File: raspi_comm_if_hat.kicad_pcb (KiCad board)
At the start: 2 copper layers, 65 x 56 mm, 18 parts, among them J1 Conn_01x04, J2 Conn_01x04, J3 Conn_01x04, J4 Conn_02x20_Odd_Even, Q1 Q_PMOS_GSD, Q2 Q_PMOS_GSD, U1 MCP25625-x-SS, Y1 Resonator_Small

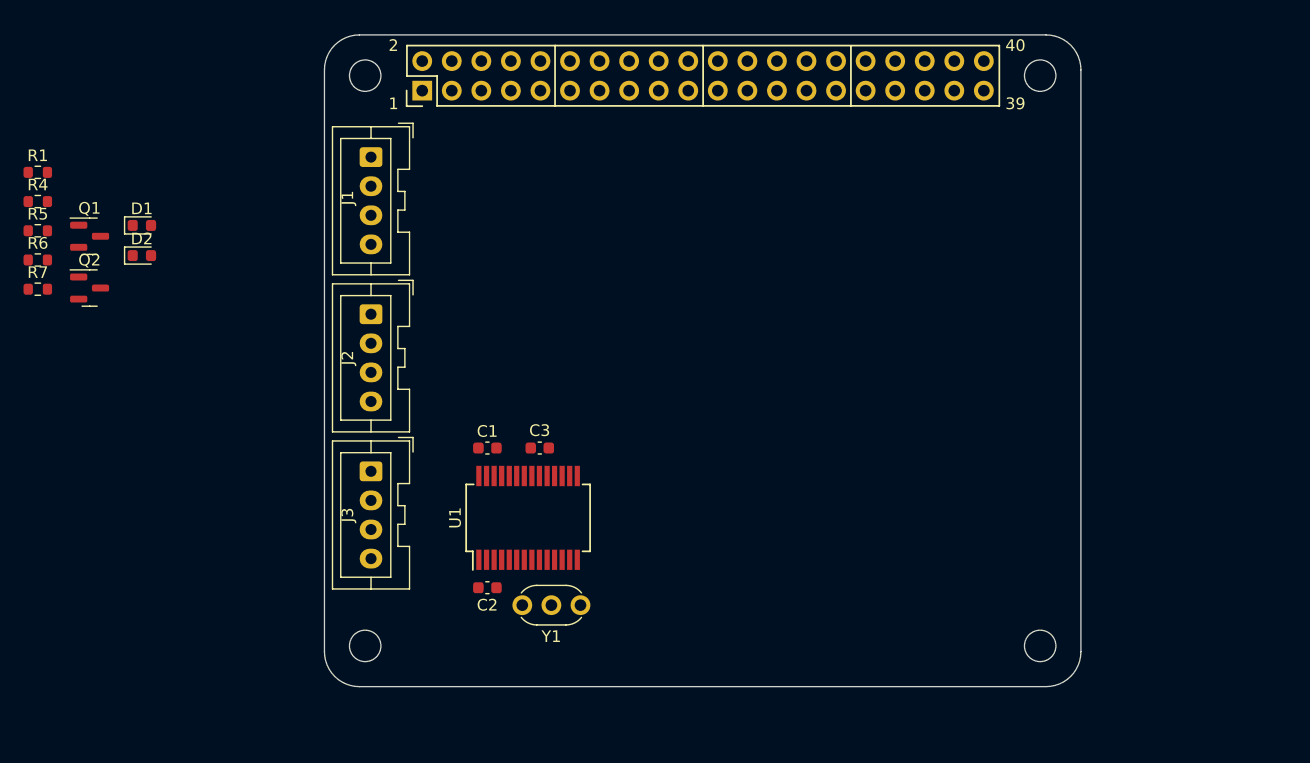
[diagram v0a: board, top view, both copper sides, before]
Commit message: draw schemtic & PCB
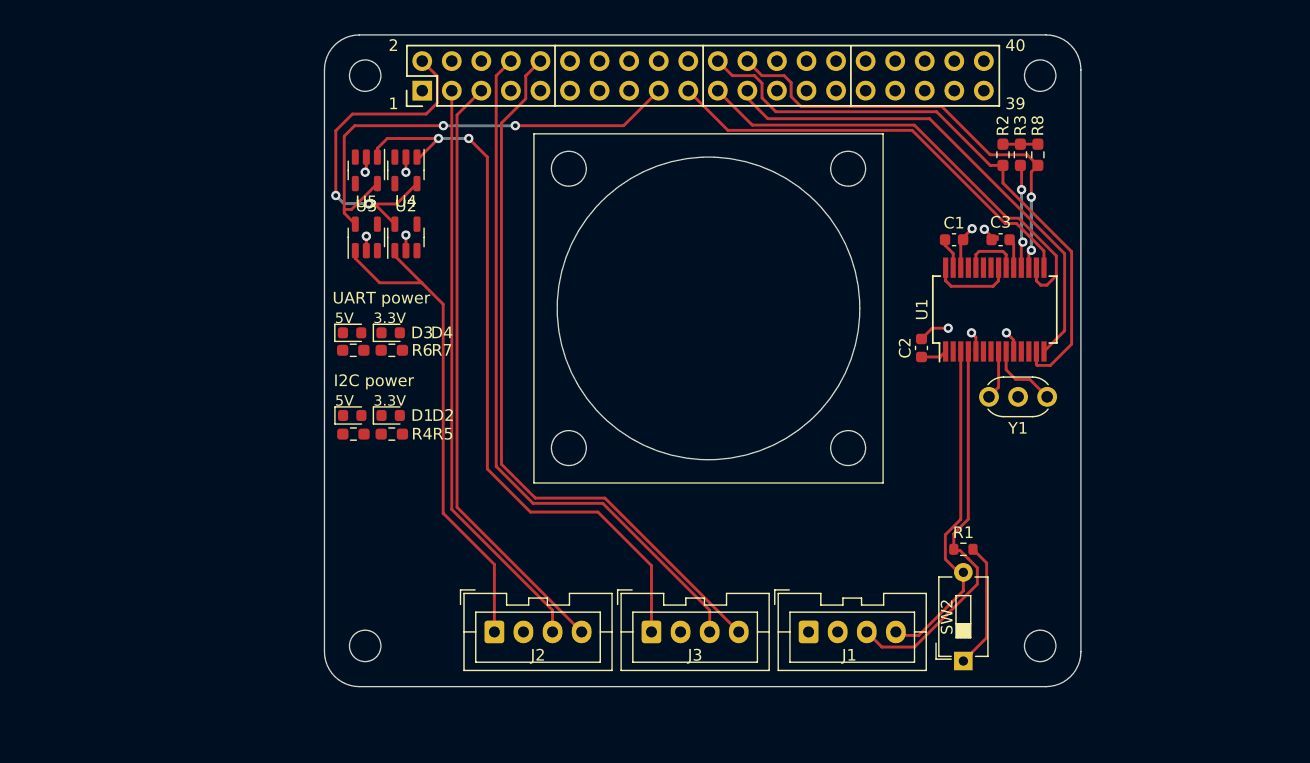
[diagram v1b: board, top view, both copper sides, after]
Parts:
- removed Q1, Q2: Q_PMOS_GSD, Package_TO_SOT_SMD:SOT-23
- added D3: LED, LED_SMD:LED_0603_1608Metric, F.Cu at (102.4, 76.6)
- added D4: LED, LED_SMD:LED_0603_1608Metric, F.Cu at (105.7, 76.6)
- added R2: 10k, Resistor_SMD:R_0603_1608Metric_Pad0.98x0.95mm_HandSolder, F.Cu at (158.3, 61.3)
- added R3: 10k, Resistor_SMD:R_0603_1608Metric_Pad0.98x0.95mm_HandSolder, F.Cu at (159.8, 61.3)
- added R8: 10k, Resistor_SMD:R_0603_1608Metric_Pad0.98x0.95mm_HandSolder, F.Cu at (161.3, 61.3)
- added SW2: SW_DIP_x01, Button_Switch_THT:SW_DIP_SPSTx01_Slide_6.7x4.1mm_W7.62mm_P2.54mm_LowProfile, F.Cu at (154.9, 104.8)
- added U2: TCK107AF, Package_TO_SOT_SMD:SOT-23-5, F.Cu at (107.0, 68.4)
- added U3: TCK107AF, Package_TO_SOT_SMD:SOT-23-5, F.Cu at (103.6, 68.4)
- added U4: TCK107AF, Package_TO_SOT_SMD:SOT-23-5, F.Cu at (107.0, 62.6)
- added U5: TCK107AF, Package_TO_SOT_SMD:SOT-23-5, F.Cu at (103.6, 62.6)
- J1, J2, J3: value Conn_01x04 -> B04B-XA
- R4, R5, R6, R7: value 4.7k -> 1k; footprint Resistor_SMD:R_0603_1608Metric -> Resistor_SMD:R_0603_1608Metric_Pad0.98x0.95mm_HandSolder
- Y1: value Resonator_Small -> 20MHz
- moved R1 85.9 mm to (154.9, 95.2)
- moved J1 55.5 mm to (141.6, 102.3), turned to 0 degrees
- moved C1 43.9 mm to (154.1, 68.6)
- moved U1 43.9 mm to (157.6, 74.6)
- moved Y1 43.9 mm to (162.1, 82.1)
- moved C3 43.5 mm to (158.1, 68.6)
- moved C2 42.6 mm to (151.3, 77.9), turned to 90 degrees
- moved R5 35.1 mm to (105.8, 85.3)
- moved R4 33.7 mm to (102.5, 85.3)
- moved R7 30.9 mm to (105.8, 78.1)
- moved J2 29.3 mm to (114.6, 102.3), turned to 0 degrees
- moved R6 28.2 mm to (102.5, 78.1)
- moved J3 27.8 mm to (128.1, 102.3), turned to 0 degrees
- moved D2 25.4 mm to (105.7, 83.7)
- moved D1 24.4 mm to (102.4, 83.7)
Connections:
- C2 pad 1: +3V3 -> +3.3V
- C3 pad 1: +3V3 -> +3.3V
- D1 pad 1: unconnected-(D1-K-Pad1) -> Net-(D1-K)
- D2 pad 1: unconnected-(D2-K-Pad1) -> Net-(D2-K)
- J1 pad 1: unconnected-(J1-Pin_1-Pad1) -> GND
- J1 pad 2: GND -> +12V
- J2 pad 1: unconnected-(J2-Pin_1-Pad1) -> I2C_PWR
- J2 pad 2: unconnected-(J2-Pin_2-Pad2) -> GND
- J2 pad 3: unconnected-(J2-Pin_3-Pad3) -> SDA
- J2 pad 4: unconnected-(J2-Pin_4-Pad4) -> SDL
- J3 pad 1: unconnected-(J3-Pin_1-Pad1) -> UART_PWR
- J3 pad 2: unconnected-(J3-Pin_2-Pad2) -> GND
- J3 pad 3: unconnected-(J3-Pin_3-Pad3) -> TX
- J3 pad 4: unconnected-(J3-Pin_4-Pad4) -> RX
- J4 pad 10: unconnected-(J4-Pin_10-Pad10) -> RX
- J4 pad 14: unconnected-(J4-Pin_14-Pad14) -> GND
- J4 pad 17: unconnected-(J4-Pin_17-Pad17) -> +3.3V
- J4 pad 19: unconnected-(J4-Pin_19-Pad19) -> MOSI
- J4 pad 2: unconnected-(J4-Pin_2-Pad2) -> +5V
- J4 pad 21: unconnected-(J4-Pin_21-Pad21) -> MISO
- J4 pad 22: unconnected-(J4-Pin_22-Pad22) -> CAN_INT
- J4 pad 23: unconnected-(J4-Pin_23-Pad23) -> CLK
- J4 pad 24: unconnected-(J4-Pin_24-Pad24) -> CS
- J4 pad 3: unconnected-(J4-Pin_3-Pad3) -> SDA
- J4 pad 34: unconnected-(J4-Pin_34-Pad34) -> GND
- J4 pad 5: unconnected-(J4-Pin_5-Pad5) -> SDL
- J4 pad 6: unconnected-(J4-Pin_6-Pad6) -> GND
- J4 pad 8: unconnected-(J4-Pin_8-Pad8) -> TX
- R4 pad 1: +5V -> Net-(D1-K)
- R4 pad 2: Net-(Q1-G) -> GND
- R5 pad 1: Net-(Q1-G) -> Net-(D2-K)
- R5 pad 2: Net-(SW1-A) -> GND
- R6 pad 1: +3V3 -> Net-(D3-K)
- R6 pad 2: Net-(Q2-G) -> GND
- R7 pad 1: Net-(Q2-G) -> Net-(D4-K)
- R7 pad 2: Net-(SW1-C) -> GND
- U1 pad 1: +3V3 -> +3.3V
- U1 pad 13: unconnected-(U1-~{INT}-Pad13) -> CAN_INT
- U1 pad 14: unconnected-(U1-SCK-Pad14) -> CLK
- U1 pad 15: unconnected-(U1-SI-Pad15) -> MOSI
- U1 pad 16: unconnected-(U1-SO-Pad16) -> MISO
- U1 pad 17: unconnected-(U1-~{CS}-Pad17) -> CS
- U1 pad 18: unconnected-(U1-~{RESET}-Pad18) -> Net-(U1-~{RESET})
- U1 pad 19: +3V3 -> +3.3V
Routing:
- net UART_PWR: track 0.00 -> 63.8 mm, vias 0 -> 2
- net RX: track 0.00 -> 62.4 mm
- net TX: track 0.00 -> 60.7 mm
- net SDL: track 0.00 -> 51.8 mm
- net CAN_INT: track 0.00 -> 51.7 mm
- net SDA: track 0.00 -> 50.1 mm
- net +3.3V: track 0.00 -> 48.2 mm, vias 0 -> 2
- net I2C_PWR: track 0.00 -> 43.5 mm
- net CLK: track 0.00 -> 42.6 mm
- net MISO: track 0.00 -> 40.0 mm
- net CS: track 0.00 -> 38.5 mm, vias 0 -> 2
- net MOSI: track 0.00 -> 37.7 mm
- net Net-(J1-Pin_3): track 0.00 -> 33.9 mm
- net +5V: track 0.00 -> 33.1 mm, vias 0 -> 2
- net Net-(J1-Pin_4): track 0.00 -> 29.5 mm
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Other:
- outline, holes or cut-outs redrawn
- board text added: "3.3V"
- board text added: "5V"
- board text added: "I2C power"
- board text added: "UART power"

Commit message: update pcb
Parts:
- added H1: MountingHole, MountingHole:MountingHole_2.7mm_M2.5, F.Cu at (103.5, 54.5)
- added H2: MountingHole, MountingHole:MountingHole_2.7mm_M2.5, F.Cu at (161.5, 54.5)
- added H3: MountingHole, MountingHole:MountingHole_2.7mm_M2.5, F.Cu at (103.5, 103.5)
- added H4: MountingHole, MountingHole:MountingHole_2.7mm_M2.5, F.Cu at (161.5, 103.5)
- added SW1: SW_SPDT, Button_Switch_THT:SW_CuK_OS102011MA1QN1_SPDT_Angled, F.Cu at (103.5, 90.3)
- added SW3: SW_SPDT, Button_Switch_THT:SW_CuK_OS102011MA1QN1_SPDT_Angled, F.Cu at (103.5, 76.7)
- U2, U3, U4, U5: value TCK107AF -> TCK106AF
- moved D2 10.5 mm to (108.7, 93.8), turned to -90 degrees
- moved D1 9.28 mm to (108.7, 90.5), turned to -90 degrees
- moved R5 8.70 mm to (107.1, 93.9), turned to -90 degrees
- moved R4 7.03 mm to (107.1, 90.6), turned to -90 degrees
- moved D3 6.25 mm to (108.6, 77.1), turned to -90 degrees
- moved D4 4.80 mm to (108.6, 80.4), turned to -90 degrees
- moved R6 4.71 mm to (107.1, 77.2), turned to -90 degrees
- moved R7 2.75 mm to (107.1, 80.5), turned to -90 degrees
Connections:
- J4 pad 1: unconnected-(J4-Pin_1-Pad1) -> +3.3V
- J4 pad 25: unconnected-(J4-Pin_25-Pad25) -> GND
- J4 pad 30: unconnected-(J4-Pin_30-Pad30) -> GND
- J4 pad 39: unconnected-(J4-Pin_39-Pad39) -> GND
- J4 pad 9: unconnected-(J4-Pin_9-Pad9) -> GND
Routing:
- net +5V: track 33.1 -> 153.5 mm, vias 2 -> 7
- net +3.3V: track 48.2 -> 89.3 mm, vias 2 -> 3
- net Net-(D1-A): track 0.00 -> 35.7 mm, vias 0 -> 2
- net Net-(D4-A): track 0.00 -> 32.9 mm, vias 0 -> 4
- net Net-(D2-A): track 0.00 -> 32.0 mm, vias 0 -> 2
- net Net-(D3-A): track 0.00 -> 24.8 mm, vias 0 -> 4
- net GND: track 16.4 -> 20.6 mm, vias 9 -> 13
- net Net-(D2-K): track 0.00 -> 1.61 mm
- net Net-(D1-K): track 0.00 -> 1.61 mm
- net Net-(D4-K): track 0.00 -> 1.51 mm
- net Net-(D3-K): track 0.00 -> 1.51 mm
- net UART_PWR: track 63.8 -> 64.5 mm
- added copper zone on B.Cu, net GND
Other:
- outline, holes or cut-outs redrawn

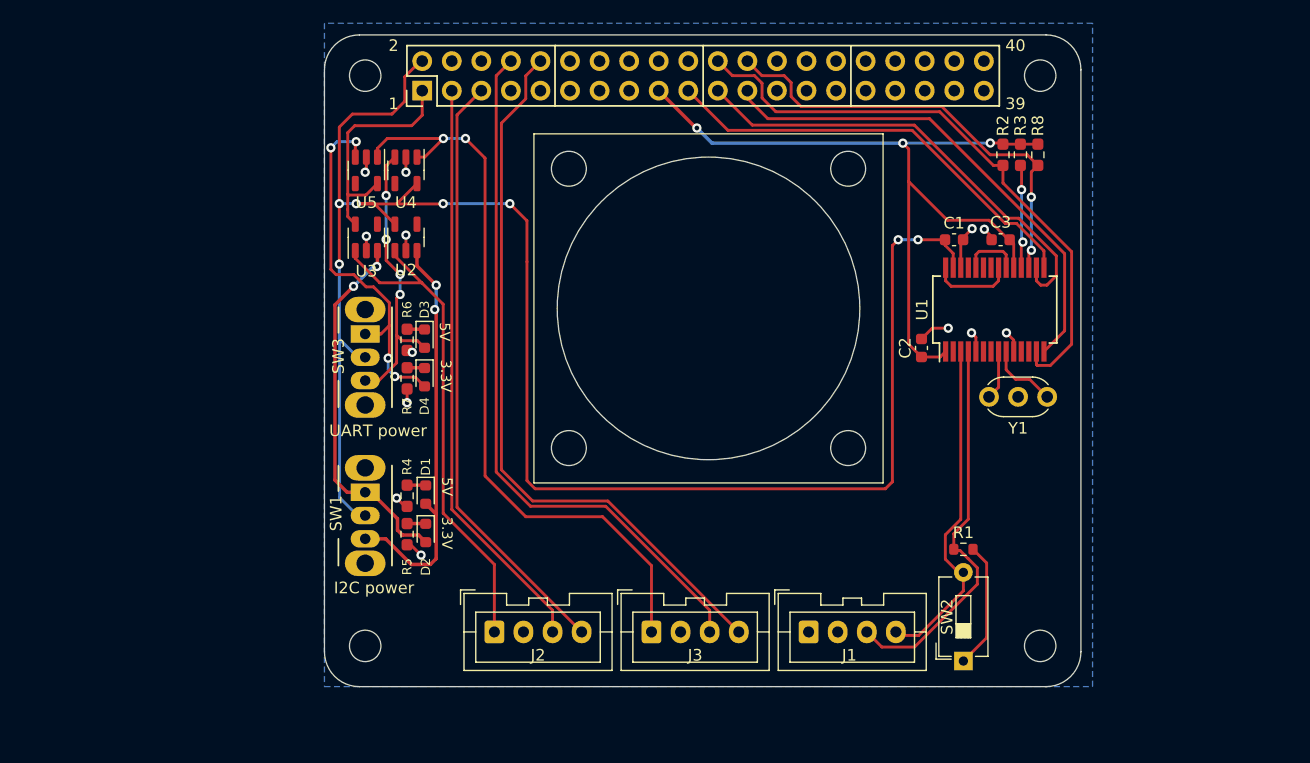
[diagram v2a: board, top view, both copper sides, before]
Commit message: add fan connector
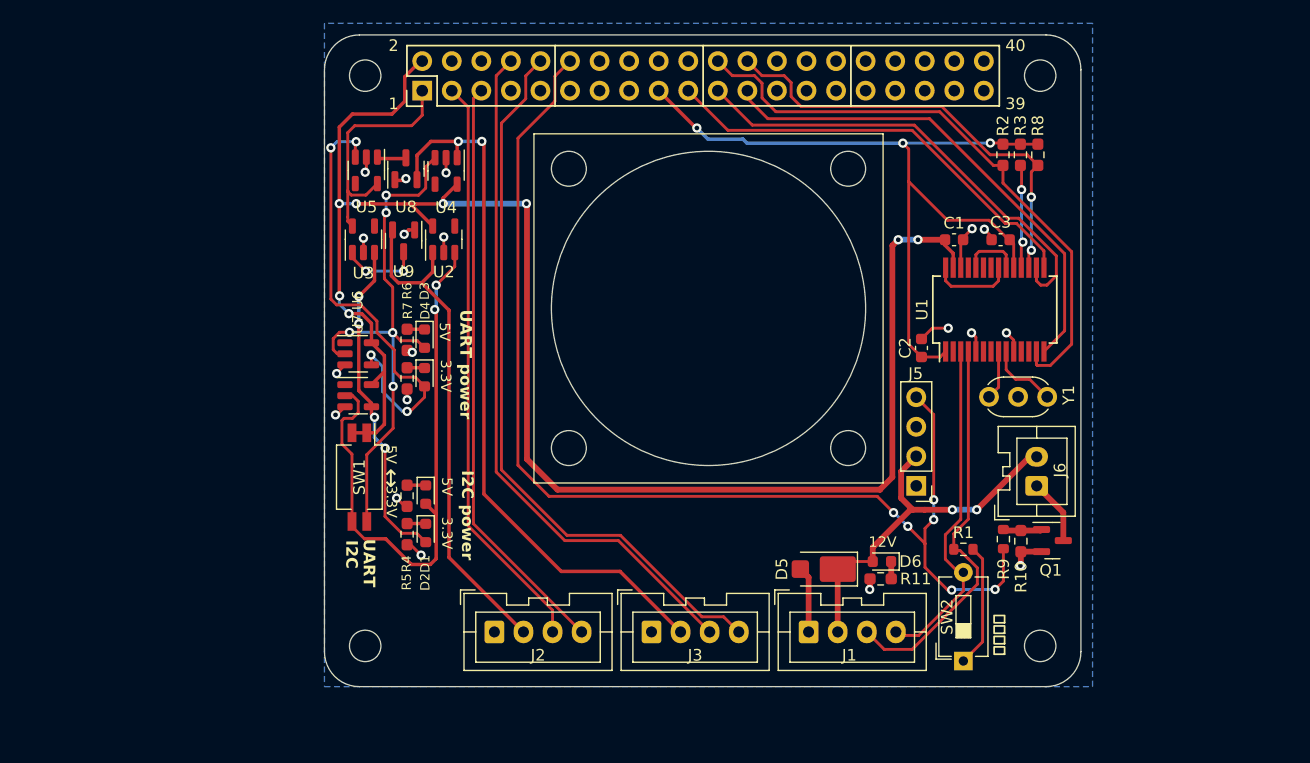
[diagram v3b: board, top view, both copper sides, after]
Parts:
- removed SW3: SW_SPDT, Button_Switch_THT:SW_CuK_OS102011MA1QN1_SPDT_Angled
- added D5: D_Schottky, Diode_SMD:Vishay_SMPA, F.Cu at (142.9, 96.9)
- added D6: LED, LED_SMD:LED_0603_1608Metric, F.Cu at (147.9, 96.2)
- added J5: Conn_01x04, Connector_PinHeader_2.54mm:PinHeader_1x04_P2.54mm_Vertical, F.Cu at (150.8, 89.8)
- added J6: Conn_01x02, Connector_JST:JST_XA_B02B-XASK-1_1x02_P2.50mm_Vertical, F.Cu at (161.2, 89.8)
- added Q1: Q_NMOS_GSD, Package_TO_SOT_SMD:SOT-23, F.Cu at (162.6, 94.5)
- added R10: 10k, Resistor_SMD:R_0603_1608Metric_Pad0.98x0.95mm_HandSolder, F.Cu at (159.8, 94.5)
- added R11: 10k, Resistor_SMD:R_0603_1608Metric_Pad0.98x0.95mm_HandSolder, F.Cu at (147.8, 97.7)
- added R9: 120, Resistor_SMD:R_0603_1608Metric, F.Cu at (158.3, 94.3)
- added U6: 74AHC1G04, Package_TO_SOT_SMD:SOT-23-5, F.Cu at (102.9, 78.4)
- added U7: 74AHC1G04, Package_TO_SOT_SMD:SOT-23-5, F.Cu at (102.9, 82.0)
- added U8: CH213K, Package_TO_SOT_SMD:SOT-23, F.Cu at (107.0, 62.5)
- added U9: CH213K, Package_TO_SOT_SMD:SOT-23, F.Cu at (106.8, 68.7)
- SW1: value SW_SPDT -> SW_DIP_x02; footprint Button_Switch_THT:SW_CuK_OS102011MA1QN1_SPDT_Angled -> Button_Switch_SMD:SW_DIP_SPSTx02_Slide_Copal_CHS-02B_W7.62mm_P1.27mm
- moved U4 3.45 mm to (110.5, 62.7)
- moved U2 3.25 mm to (110.2, 68.6)
- moved SW1 1.39 mm to (103.0, 89.0)
- moved U3 0.30 mm to (103.3, 68.6)
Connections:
- J2 pad 1: I2C_PWR -> GND
- J2 pad 2: GND -> I2C_PWR
- J3 pad 1: UART_PWR -> GND
- J3 pad 2: GND -> UART_PWR
- J4 pad 12: unconnected-(J4-Pin_12-Pad12) -> FAN_PWM
- SW1 pad 1: Net-(D2-A) -> +5V
- U3 pad 1: I2C_PWR -> Net-(U3-OUT)
- U5 pad 1: UART_PWR -> Net-(U5-OUT)
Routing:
- net FAN_PWM: track 0.00 -> 100.6 mm, vias 0 -> 6
- net +12V: track 0.00 -> 32.7 mm, vias 0 -> 2
- net Net-(D3-A): track 24.8 -> 46.9 mm, vias 4 -> 5
- net Net-(D1-A): track 35.7 -> 51.0 mm
- net GND: track 20.6 -> 34.2 mm, vias 13 -> 19
- net Net-(U3-OUT): track 0.00 -> 7.07 mm, vias 0 -> 2
- net Net-(D4-A): track 32.9 -> 39.8 mm
- net Net-(J6-Pin_1): track 0.00 -> 5.65 mm
- net +5V: track 153.5 -> 148.0 mm, vias 7 -> 8
- net Net-(D2-A): track 32.0 -> 28.6 mm, vias 2 -> 4
- net Net-(Q1-G): track 0.00 -> 3.35 mm
- net UART_PWR: track 64.5 -> 61.8 mm
- net Net-(U5-OUT): track 0.00 -> 2.50 mm
- net Net-(D6-K): track 0.00 -> 1.50 mm
- net SDL: track 51.8 -> 50.6 mm
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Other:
- outline, holes or cut-outs redrawn
- board text added: "12V"
- board text added: "I2C"
- board text added: "UART"
- board text added: "↔"
- board text added: "終端抵抗"

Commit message: v0.1.0
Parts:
- added C1: 10uF, Capacitor_SMD:C_0603_1608Metric, F.Cu at (104.0, 61.5)
- added C2: 10uF, Capacitor_SMD:C_0603_1608Metric, F.Cu at (108.9, 61.5)
- added C3: 0.1uF, Capacitor_SMD:C_0603_1608Metric, F.Cu at (114.4, 92.8)
- added C4: 100uF, Capacitor_Tantalum_SMD:CP_EIA-7343-15_Kemet-W, F.Cu at (141.5, 95.9)
- added C8: 0.1uF, Capacitor_SMD:C_0603_1608Metric, F.Cu at (110.8, 100.8)
- added C9: 0.1uF, Capacitor_SMD:C_0603_1608Metric, F.Cu at (124.5, 100.5)
- added Q2: Q_NMOS_GSD, Package_TO_SOT_SMD:SOT-23, F.Cu at (117.5, 99.8)
- added Q3: Q_NMOS_GSD, Package_TO_SOT_SMD:SOT-23, F.Cu at (117.5, 96.5)
- added Q4: Q_NMOS_GSD, Package_TO_SOT_SMD:SOT-23, F.Cu at (131.0, 99.9)
- added Q5: Q_NMOS_GSD, Package_TO_SOT_SMD:SOT-23, F.Cu at (131.0, 96.5)
- added R14: 10k, Resistor_SMD:R_0603_1608Metric_Pad0.98x0.95mm_HandSolder, F.Cu at (114.8, 96.5)
- added R15: 10k, Resistor_SMD:R_0603_1608Metric_Pad0.98x0.95mm_HandSolder, F.Cu at (114.8, 99.9)
- added R16: 10k, Resistor_SMD:R_0603_1608Metric_Pad0.98x0.95mm_HandSolder, F.Cu at (120.2, 99.9)
- added R17: 10k, Resistor_SMD:R_0603_1608Metric_Pad0.98x0.95mm_HandSolder, F.Cu at (120.2, 96.5)
- added R18: 10k, Resistor_SMD:R_0603_1608Metric_Pad0.98x0.95mm_HandSolder, F.Cu at (128.4, 96.5)
- added R19: 10k, Resistor_SMD:R_0603_1608Metric_Pad0.98x0.95mm_HandSolder, F.Cu at (128.4, 100.0)
- added R20: 10k, Resistor_SMD:R_0603_1608Metric_Pad0.98x0.95mm_HandSolder, F.Cu at (133.7, 100.0)
- added R21: 10k, Resistor_SMD:R_0603_1608Metric_Pad0.98x0.95mm_HandSolder, F.Cu at (133.7, 96.5)
- added R7: 10k, Resistor_SMD:R_0603_1608Metric_Pad0.98x0.95mm_HandSolder, F.Cu at (110.6, 99.2)
- added R8: 10k, Resistor_SMD:R_0603_1608Metric_Pad0.98x0.95mm_HandSolder, F.Cu at (124.3, 99.0)
- added REF**: KiCad-Logo2_5mm_SilkScreen, Symbol:KiCad-Logo2_5mm_SilkScreen, F.Cu at (156.7, 67.7)
- moved SW2 3.07 mm to (102.3, 92.0)
- moved C5 3.00 mm to (158.1, 71.6)
- moved C6 3.00 mm to (151.3, 80.9)
- moved C7 3.00 mm to (154.1, 71.6)
- moved D1 3.00 mm to (147.9, 99.2)
- moved D2 3.00 mm to (142.9, 99.9)
- moved D5 3.00 mm to (108.6, 80.1)
- moved D6 3.00 mm to (108.6, 83.4)
- moved H1 3.00 mm to (103.5, 57.5)
- moved H2 3.00 mm to (161.5, 57.5)
- moved H3 3.00 mm to (103.5, 106.5)
- moved H4 3.00 mm to (161.5, 106.5)
- moved J1 3.00 mm to (141.6, 105.3)
- moved J2 3.00 mm to (108.4, 58.8)
- moved J3 3.00 mm to (114.6, 105.3)
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- renumbered C3 to C5, C2 to C6, C1 to C7, D6 to D1, D5 to D2, D1 to D3, D2 to D4, D3 to D5, D4 to D6, J4 to J2, J2 to J3, J6 to J4, J3 to J6, R11 to R1, R4 to R10, R5 to R11, R6 to R12, R7 to R13, R8 to R4, R1 to R5, R9 to R6, R10 to R9, SW2 to SW1, SW1 to SW2, U7 to U2, U6 to U3, U2 to U4, U4 to U5, U9 to U6, U8 to U7, U3 to U8, U5 to U9
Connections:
- J3 pad 3: SDA -> SDA_conn
- J3 pad 4: SDL -> SDL_conn
- J6 pad 3: TX -> TX_conn
- J6 pad 4: RX -> RX_conn
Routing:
- net +3.3V: track 89.6 -> 163.1 mm, vias 3 -> 11
- net I2C_PWR: track 43.5 -> 58.7 mm, vias 0 -> 4
- net UART_PWR: track 61.8 -> 75.2 mm, vias 2 -> 6
- net GND: track 34.2 -> 47.3 mm, vias 19 -> 142
- net RX_conn: track 0.00 -> 11.7 mm
- net SDL_conn: track 0.00 -> 10.8 mm
- net RX: track 62.7 -> 53.2 mm
- net SDL: track 50.6 -> 41.6 mm
- net TX_conn: track 0.00 -> 7.41 mm
- net SDA_conn: track 0.00 -> 6.87 mm
- net +5V: track 148.0 -> 142.5 mm
- net TX: track 59.9 -> 54.5 mm
- net SDA: track 50.1 -> 45.4 mm
- net +12V: track 32.7 -> 37.4 mm
- net Net-(D4-A): track 28.6 -> 25.0 mm
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- added copper zone on F.Cu, net GND
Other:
- board text added: "30mm Fan"
- board text added: "CAN"
- board text added: "DC Fan"
- board text added: "Desinged by Mochizuki12"
- board text added: "PC Fan"
- board text added: "Raspi_comm_if_hat v0.1.0"
